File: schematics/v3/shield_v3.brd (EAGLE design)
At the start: 41 x 50 mm, 34 parts, among them Q2 PMV20EN, Q3 PMV20EN, Q4 PMV20EN, Q5 PMV20EN, U1 ATMEGA168

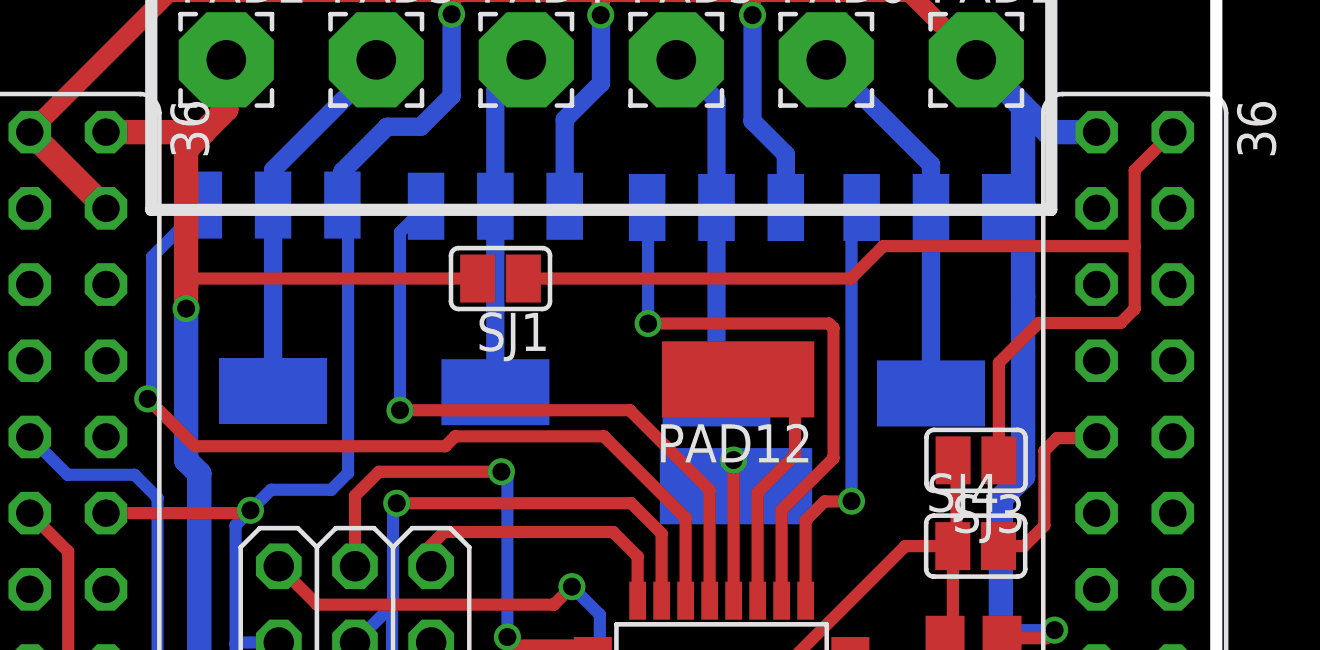
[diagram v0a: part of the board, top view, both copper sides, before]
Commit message: Added jumper to drive atmega via Vin or CHIP 5V or CHIP3.3V
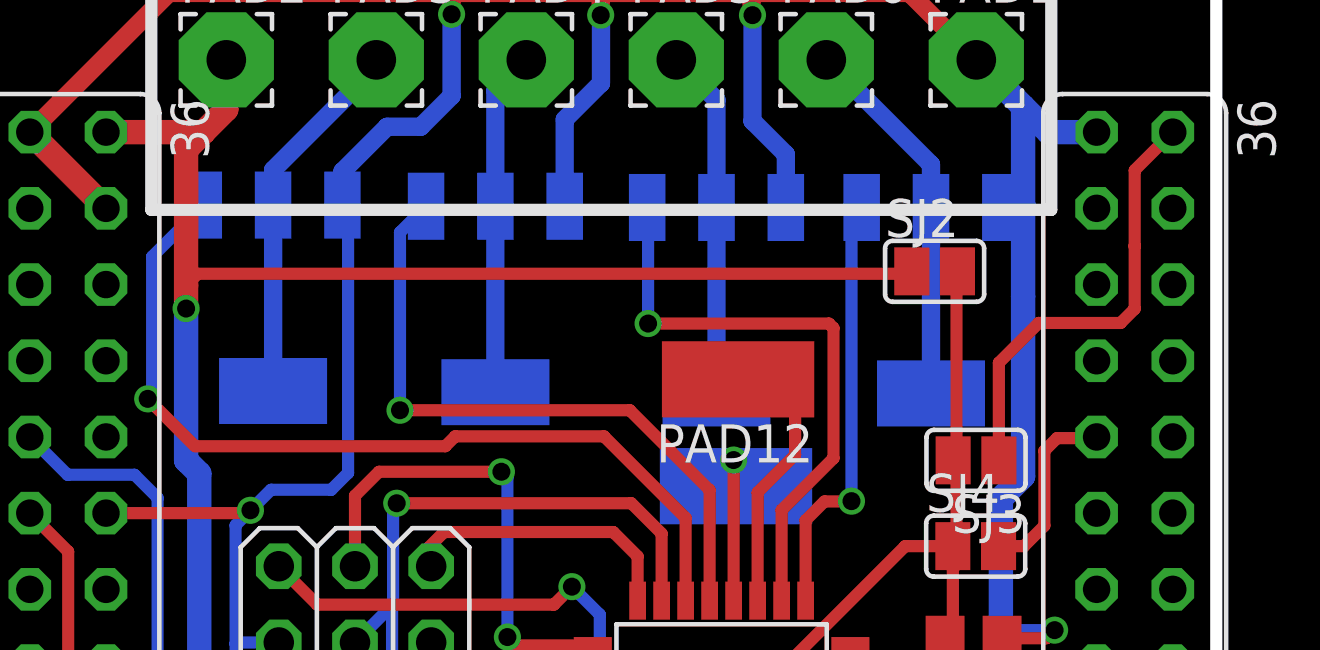
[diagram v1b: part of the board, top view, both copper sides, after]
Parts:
- removed SJ1: (no value), jumper:SJ
- added SJ2: (no value), jumper:SJ
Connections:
- net 5V: no longer SJ1.1
- net VCC: now also SJ2.2
- net VIN: now also SJ2.1; no longer SJ1.2
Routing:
- net 5V: track 35.8 -> 15.0 mm
- net VIN: track 58.2 -> 73.1 mm
- net VCC: track 63.4 -> 69.8 mm
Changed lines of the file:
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@@
 <?xml version="1.0" encoding="utf-8"?>
 <!DOCTYPE eagle SYSTEM "eagle.dtd">
-<eagle version="6.5.0">
+<eagle version="7.5.0">
 <drawing>
 <settings>
@@
 <pass name="Default">
 <param name="RoutingGrid" value="50mil"/>
+<param name="AutoGrid" value="1"/>
+<param name="Efforts" value="0"/>
+<param name="TopRouterVariant" value="1"/>
 <param name="tpViaShape" value="round"/>
 <param name="PrefDir.1" value="|"/>
@@
 <element name="SJ3" library="jumper" package="SJ" value="" x="32.99" y="33.65" rot="R180"/>
 <element name="SJ4" library="jumper" package="SJ" value="" x="32.98" y="30.79"/>
-<element name="SJ1" library="jumper" package="SJ" value="" x="17.14" y="39.71" rot="R180"/>
 <element name="PAD8" library="wirepad" package="SMD2,54-5,08" value="" x="24.99" y="32.79" rot="MR270"/>
 <element name="PAD12" library="wirepad" package="SMD2,54-5,08" value="" x="25.06" y="36.35" rot="R90"/>
 <element name="PAD13" library="wirepad" package="SMD1,27-2,54" value="" x="32.39" y="20.74" rot="R90"/>
 <element name="R2" library="rcl" package="M1206" value="" x="25.77" y="18.75" rot="MR180"/>
+<element name="SJ2" library="jumper" package="SJ" value="" x="31.61" y="39.95"/>
 </elements>
 <signals>
@@
 <wire x1="15.64" y1="26.23" x2="14.83" y2="27.04" width="0.4064" layer="1"/>
 <wire x1="14.83" y1="27.04" x2="14.83" y2="27.58" width="0.4064" layer="1"/>
+<contactref element="SJ2" pad="2"/>
+<wire x1="32.34" y1="33.538" x2="32.34" y2="39.918" width="0.4064" layer="1"/>
+<wire x1="32.34" y1="39.918" x2="32.372" y2="39.95" width="0.4064" layer="1"/>
 </signal>
 <signal name="OC0_PWM1">
@@
 <wire x1="6.66" y1="33.65" x2="6.66" y2="38.71" width="0.8128" layer="16"/>
 <wire x1="7.1" y1="33.21" x2="6.66" y2="33.65" width="0.8128" layer="16"/>
-<contactref element="SJ1" pad="2"/>
-<wire x1="16.378" y1="39.71" x2="6.89" y2="39.71" width="0.4064" layer="1"/>
-<wire x1="6.89" y1="39.71" x2="6.66" y2="39.48" width="0.4064" layer="1"/>
+<wire x1="7.05" y1="39.87" x2="6.66" y2="39.48" width="0.4064" layer="1"/>
+<contactref element="SJ2" pad="1"/>
+<wire x1="30.848" y1="39.95" x2="30.458" y2="39.84" width="0.4064" layer="1"/>
+<wire x1="7.05" y1="39.87" x2="30.768" y2="39.87" width="0.4064" layer="1"/>
+<wire x1="30.768" y1="39.87" x2="30.848" y2="39.95" width="0.4064" layer="1"/>
 </signal>
 <signal name="_5V">
@@
 <wire x1="38.28" y1="40.8" x2="38.28" y2="43.32" width="0.4064" layer="1"/>
 <wire x1="38.28" y1="43.32" x2="39.55" y2="44.59" width="0.4064" layer="1"/>
-<contactref element="SJ1" pad="1"/>
-<wire x1="17.902" y1="39.71" x2="28.82" y2="39.71" width="0.4064" layer="1"/>
-<wire x1="28.82" y1="39.71" x2="29.9" y2="40.79" width="0.4064" layer="1"/>
-<wire x1="29.9" y1="40.79" x2="38.27" y2="40.79" width="0.4064" layer="1"/>
 <wire x1="38.27" y1="40.79" x2="38.28" y2="40.8" width="0.4064" layer="1" curve="90"/>
 </signal>
